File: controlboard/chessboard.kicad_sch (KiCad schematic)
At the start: 9 parts, among them J10 Conn_01x08

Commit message: more progress on controlboard pcb
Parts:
- added D14, D15: WS2812B, LED_SMD:LED_WS2812B_PLCC4_5.0x5.0mm_P3.2mm, symbol LED:WS2812B
- added JP18, JP8: SolderJumper_2_Open, symbol Jumper:SolderJumper_2_Open
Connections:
- net 5V: now also D14.1 (VDD), D15.1 (VDD)
- net GND: now also D14.3 (VSS), D15.3 (VSS)
- net LED_IN: now also D14.4 (DIN), D15.2 (DOUT), JP18.2 (B), JP8.1 (A)
- new net: D14.2 (DOUT), D15.4 (DIN), JP18.1 (A), JP8.2 (B)
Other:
- note added: "3.3V: 64 * 5mA + 8 * 20mA = 480mA"
- note added: "Max: 5V 68 * 36mA = 2.5A Nom: 5V 68 * 12mA = .9A"
- note added: "two more at the end cuz we're cool 😎 + can you ever have too much RGB?"
- note added: "two pixels onboard for debugging/status stuff"

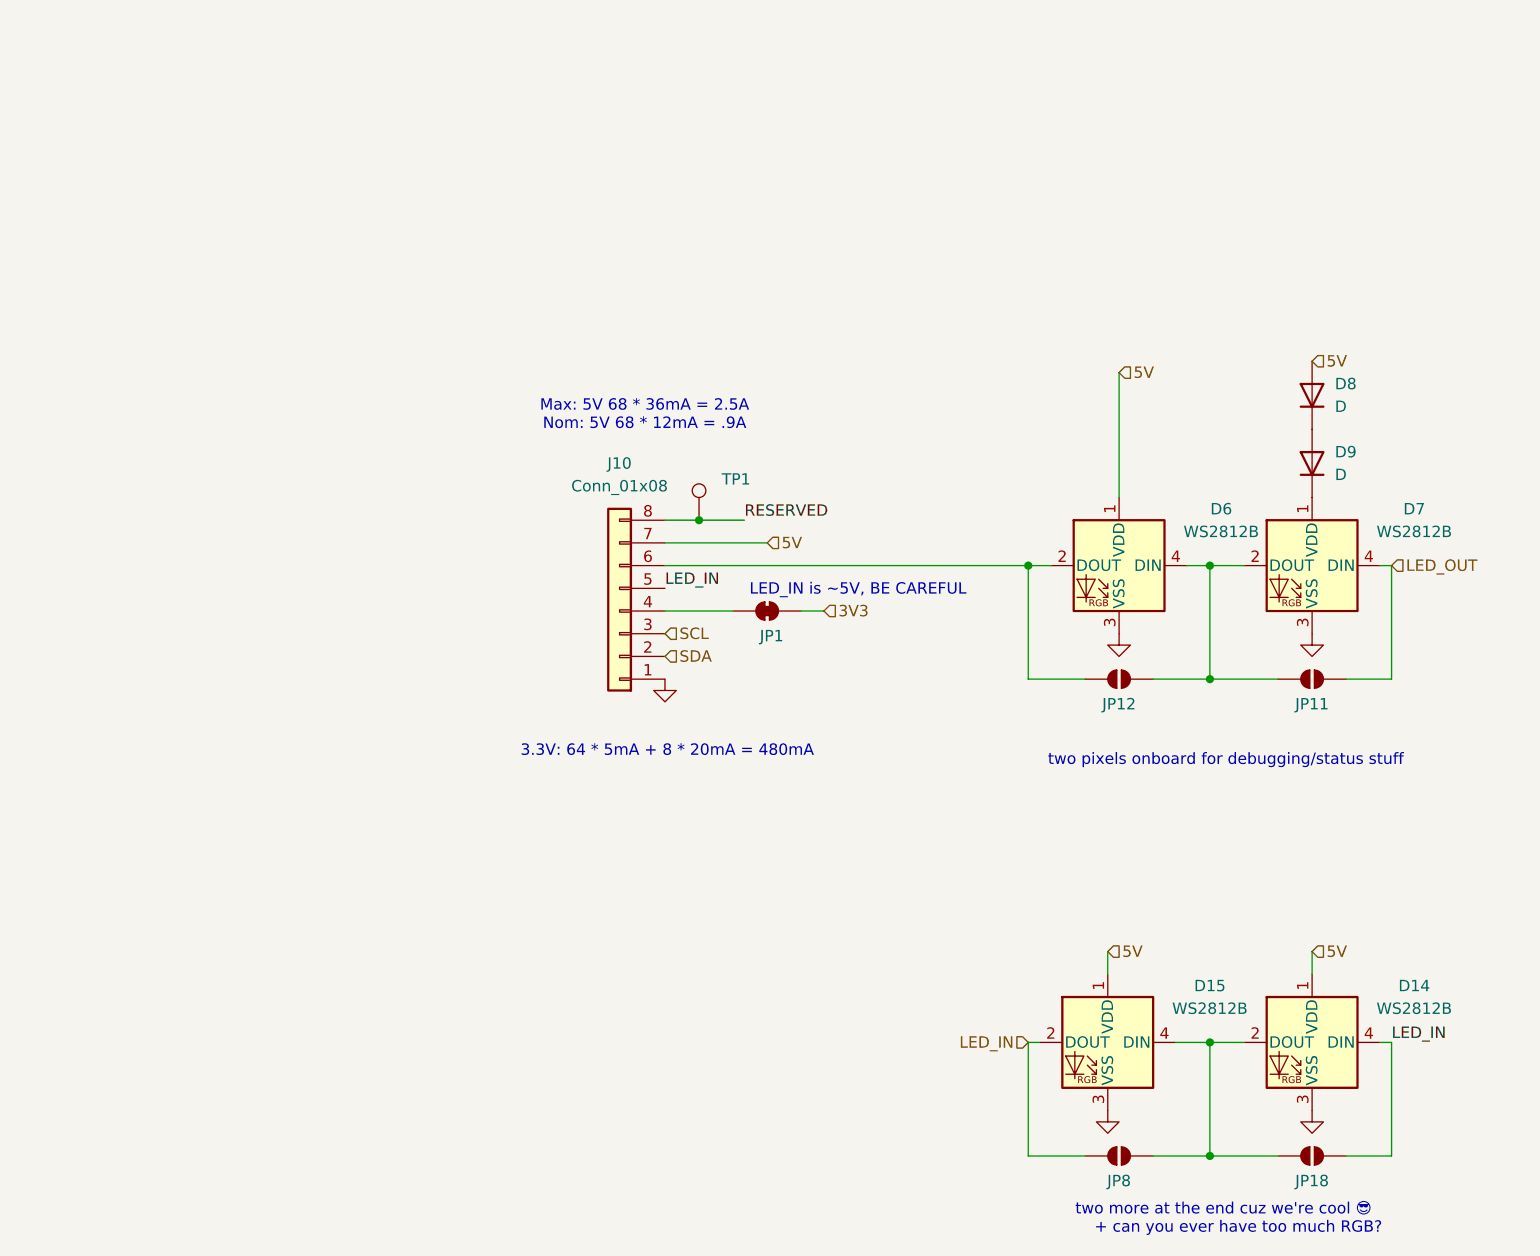
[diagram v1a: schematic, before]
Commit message: ControlBoard Schematic nearly done
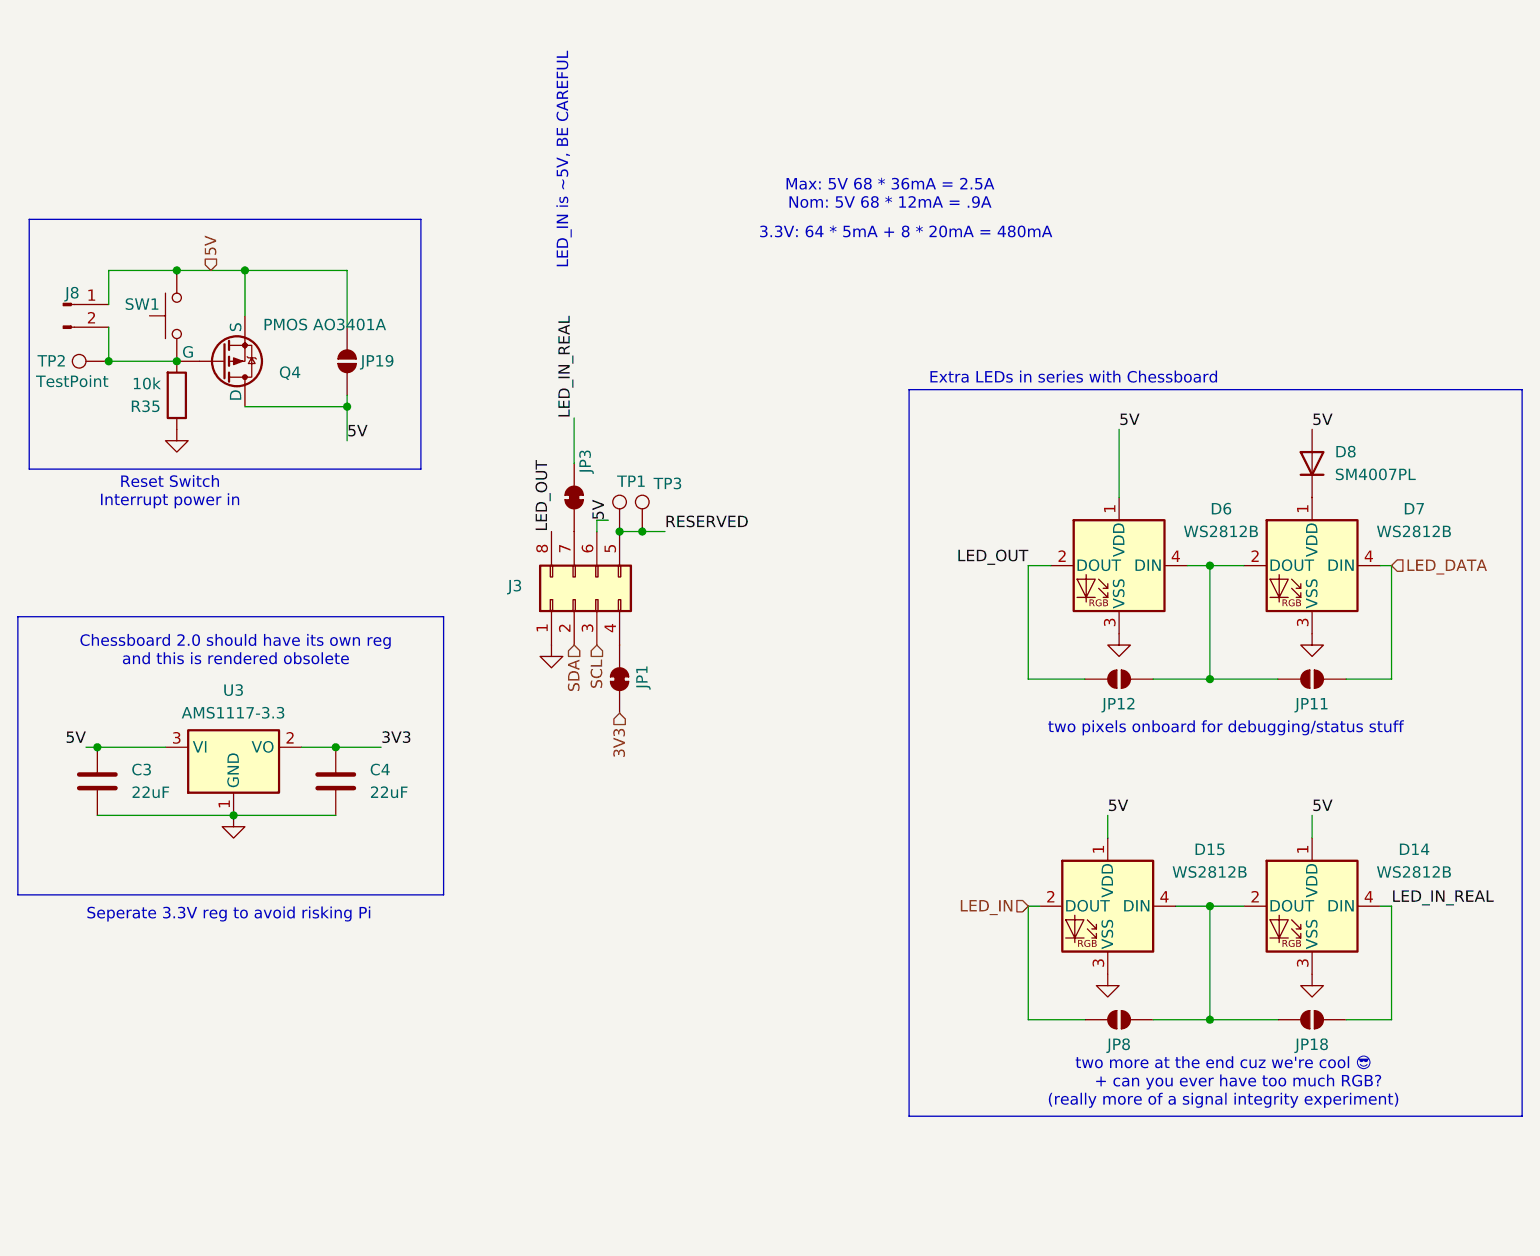
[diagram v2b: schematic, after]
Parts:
- removed D9: D, symbol Device:D
- removed J10: Conn_01x08, symbol Connector_Generic:Conn_01x08
- added C3, C4: 22uF, Capacitor_SMD:C_1206_3216Metric_Pad1.33x1.80mm_HandSolder, symbol Device:C
- added J3: Conn_02x04_Counter_Clockwise, Connector_PinSocket_2.54mm:PinSocket_2x04_P2.54mm_Horizontal, symbol Connector_Generic:Conn_02x04_Counter_Clockwise
- added J8: Conn_01x02_Pin, Connector_PinHeader_2.54mm:PinHeader_1x02_P2.54mm_Vertical, symbol Connector:Conn_01x02_Pin
- added JP19: SolderJumper_2_Open, Jumper:SolderJumper-2_P1.3mm_Open_RoundedPad1.0x1.5mm, symbol Jumper:SolderJumper_2_Open
- added JP3: SolderJumper_2_Bridged, Jumper:SolderJumper-2_P1.3mm_Bridged2Bar_RoundedPad1.0x1.5mm, symbol Jumper:SolderJumper_2_Bridged
- added Q4: PMOS AO3401A, Package_TO_SOT_SMD:SOT-23_Handsoldering, symbol Simulation_SPICE:PMOS
- added R35: 10k, Resistor_SMD:R_0603_1608Metric_Pad0.98x0.95mm_HandSolder, symbol Device:R
- added SW1: SW_Push TODO FP CHECK, Button_Switch_SMD:SW_SPST_SKQG_WithStem, symbol Switch:SW_Push
- added TP2, TP3: TestPoint, Connector_PinSocket_2.54mm:PinSocket_1x01_P2.54mm_Vertical, symbol Connector:TestPoint
- added U3: AMS1117-3.3, Package_TO_SOT_SMD:SOT-223-3_TabPin2, symbol Regulator_Linear:AMS1117-3.3
- D8: value D -> SM4007PL; footprint (none) -> Diode_SMD:Nexperia_CFP3_SOD-123W
- JP1: footprint (none) -> Jumper:SolderJumper-2_P1.3mm_Bridged2Bar_RoundedPad1.0x1.5mm
- JP11, JP12, JP18, JP8: footprint (none) -> Jumper:SolderJumper-2_P1.3mm_Open_RoundedPad1.0x1.5mm
- TP1: footprint (none) -> Connector_PinSocket_2.54mm:PinSocket_1x01_P2.54mm_Vertical
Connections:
- net 3V3: now also C4.1, U3.2 (VO)
- net 5V: now also C3.1, J3.6 (Pin_6), J8.1 (Pin_1), JP19.1 (A), JP19.2 (B), Q4.1 (D), Q4.3 (S), SW1.2, U3.3 (VI)
- net GND: now also C3.2, C4.2, J3.1 (Pin_1), R35.1, U3.1 (GND)
- net LED_IN: no longer D14.4 (DIN), JP18.2 (B)
- net LED_OUT: now also D6.2 (DOUT), JP12.1 (A), J3.8 (Pin_8); no longer D7.4 (DIN), JP11.2 (B)
- net RESERVED: now also J3.5 (Pin_5), TP3.1
- net SCL: now also J3.3 (Pin_3)
- net SDA: now also J3.2 (Pin_2)
- net at JP1.1 (A): now also J3.4 (Pin_4)
- net at D8.1 (K): now also D7.1 (VDD)
- new net: J3.7 (Pin_7), JP3.2 (B)
- new net: J8.2 (Pin_2), Q4.2 (G), R35.2, SW1.1, TP2.1
- new net LED_DATA: D7.4 (DIN), JP11.2 (B)
- new net LED_IN_REAL: D14.4 (DIN), JP18.2 (B), JP3.1 (A)
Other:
- note added: "Chessboard 2.0 should have its own reg and this is rendered obsolete"
- note added: "Extra LEDs in series with Chessboard"
- note added: "Reset Switch Interrupt power in"
- note added: "Seperate 3.3V reg to avoid risking Pi"
- note added: "two more at the end cuz we're cool 😎 + can you ever have too much RGB? (really more of a signal integrity experiment)"
- note removed: "two more at the end cuz we're cool 😎 + can you ever have too much RGB?"
- moved on the sheet: D14, D15, D8, JP1, JP18, JP8, TP1

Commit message: schematic improvements
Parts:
- removed J8: Conn_01x02_Pin, Connector_PinHeader_2.54mm:PinHeader_1x02_P2.54mm_Vertical, symbol Connector:Conn_01x02_Pin
- removed JP19: SolderJumper_2_Open, Jumper:SolderJumper-2_P1.3mm_Open_RoundedPad1.0x1.5mm, symbol Jumper:SolderJumper_2_Open
- removed Q4: PMOS AO3401A, Package_TO_SOT_SMD:SOT-23_Handsoldering, symbol Simulation_SPICE:PMOS
- removed R35: 10k, Resistor_SMD:R_0603_1608Metric_Pad0.98x0.95mm_HandSolder, symbol Device:R
- removed SW1: SW_Push TODO FP CHECK, Button_Switch_SMD:SW_SPST_SKQG_WithStem, symbol Switch:SW_Push
- removed TP2: TestPoint, Connector_PinSocket_2.54mm:PinSocket_1x01_P2.54mm_Vertical, symbol Connector:TestPoint
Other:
- note removed: "Reset Switch Interrupt power in"

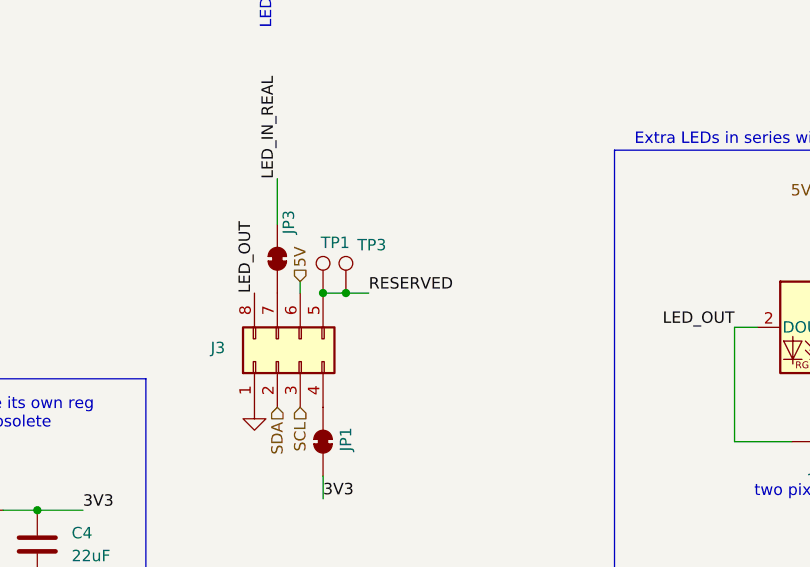
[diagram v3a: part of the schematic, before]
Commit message: improve pinout
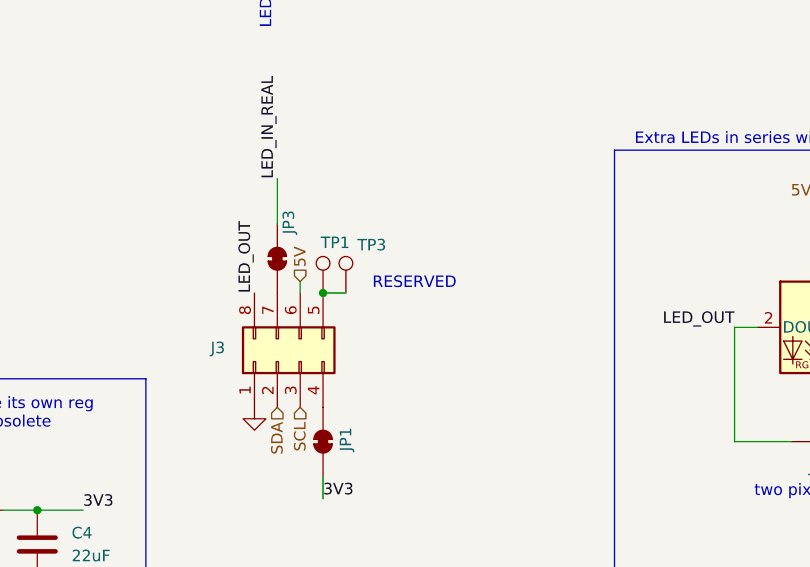
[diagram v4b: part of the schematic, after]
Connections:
- net RESERVED: no longer names the net of J3.5 (Pin_5), TP1.1, TP3.1
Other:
- note added: "RESERVED"
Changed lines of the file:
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@@
 		(color 0 0 0 0)
 	)
-	(junction
-		(at 176.53 71.12)
-		(diameter 0)
-		(color 0 0 0 0)
-	)
 	(wire
 		(pts
@@
 		(pts
 			(xy 233.68 125.73) (xy 240.03 125.73)
-		)
-		(stroke
-			(width 0)
-			(type default)
-		)
-	)
-	(wire
-		(pts
-			(xy 179.07 71.12) (xy 176.53 71.12)
 		)
 		(stroke
@@
 		)
 	)
+	(text "RESERVED"
+		(exclude_from_sim no)
+		(at 184.15 70.104 0)
+		(effects
+			(font
+				(size 1.27 1.27)
+			)
+		)
+	)
 	(text "3.3V: 64 * 5mA + 8 * 20mA = 480mA"
 		(exclude_from_sim no)
@@
 		(fields_autoplaced yes)
 		(effects
-			(font
-				(size 1.27 1.27)
-			)
-			(justify left bottom)
-		)
-	)
-	(label "RESERVED"
-		(at 179.07 71.12 0)
-		(fields_autoplaced yes)
-		(effects

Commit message: progress
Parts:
- removed JP3: SolderJumper_2_Bridged, Jumper:SolderJumper-2_P1.3mm_Bridged2Bar_RoundedPad1.0x1.5mm, symbol Jumper:SolderJumper_2_Bridged
- added C15: 100u, Capacitor_SMD:CP_Elec_6.3x5.4, symbol Device:C_Polarized
- added R12, R21: 1k, Resistor_SMD:R_0603_1608Metric_Pad0.98x0.95mm_HandSolder, symbol Device:R
- J3: symbol Connector_Generic:Conn_02x04_Counter_Clockwise -> Connector_Generic:Conn_02x04_Odd_Even
- TP1, TP3: footprint Connector_PinSocket_2.54mm:PinSocket_1x01_P2.54mm_Vertical -> Connector_PinHeader_1.00mm:PinHeader_1x01_P1.00mm_Vertical
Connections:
- net 5V: now also C15.1
- net GND: now also C15.2
- net LED_IN_REAL: now also R21.2
- net LED_OUT: now also J3.2 (Pin_2), R12.1; no longer D6.2 (DOUT), J3.8 (Pin_8), JP12.1 (A)
- net SCL: now also J3.5 (Pin_5); no longer J3.3 (Pin_3)
- net SDA: now also J3.3 (Pin_3); no longer J3.2 (Pin_2)
- net at JP1.1 (A): now also J3.7 (Pin_7); no longer J3.4 (Pin_4)
- net at TP1.1, TP3.1: now also J3.8 (Pin_8); no longer J3.5 (Pin_5)
- new net: D6.2 (DOUT), JP12.1 (A), R12.2
- new net: J3.4 (Pin_4), R21.1

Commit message: yay its all connected
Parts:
- TP1, TP3: footprint Connector_PinHeader_1.00mm:PinHeader_1x01_P1.00mm_Vertical -> TestPoint:TestPoint_THTPad_1.0x1.0mm_Drill0.5mm
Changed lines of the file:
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@@
 			)
 		)
-		(property "Footprint" "Connector_PinHeader_1.00mm:PinHeader_1x01_P1.00mm_Vertical"
+		(property "Footprint" "TestPoint:TestPoint_THTPad_1.0x1.0mm_Drill0.5mm"
 			(at 179.07 71.12 0)
 			(effects
@@
 			)
 		)
-		(property "Footprint" "Connector_PinHeader_1.00mm:PinHeader_1x01_P1.00mm_Vertical"
+		(property "Footprint" "TestPoint:TestPoint_THTPad_1.0x1.0mm_Drill0.5mm"
 			(at 181.61 71.12 0)
 			(effects

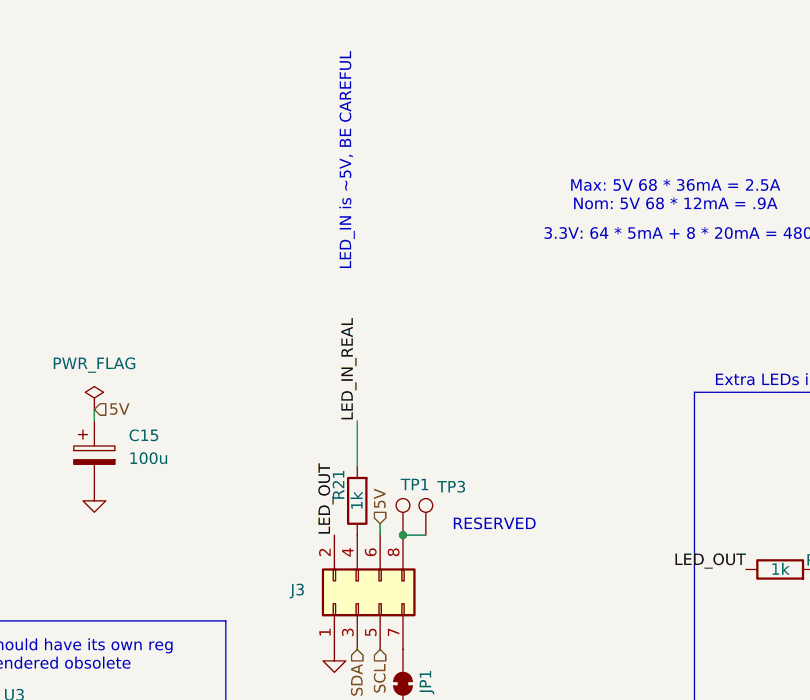
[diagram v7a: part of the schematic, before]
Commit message: controlboard: fix critical mosfet errors
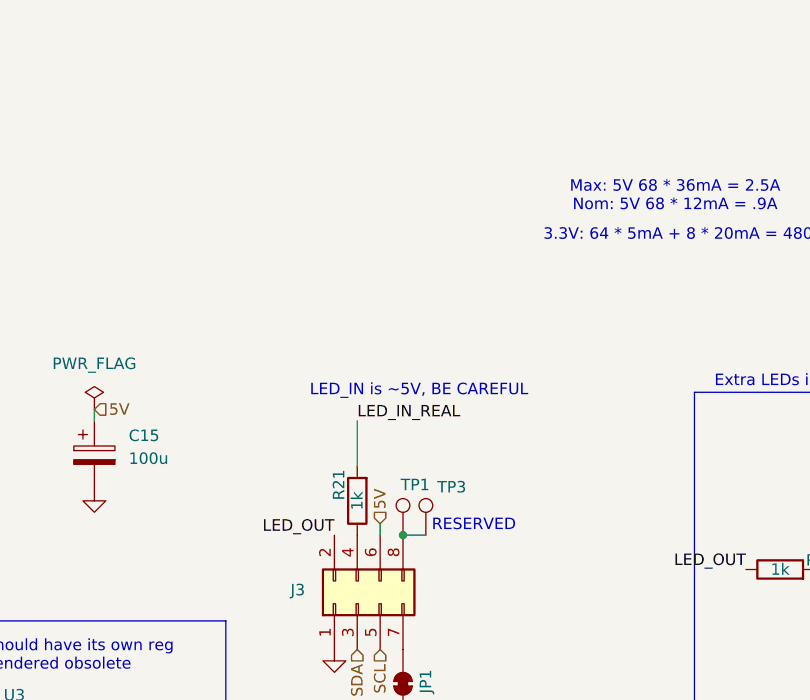
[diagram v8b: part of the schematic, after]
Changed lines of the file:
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@@
 	(text "RESERVED"
 		(exclude_from_sim no)
-		(at 184.15 70.104 0)
+		(at 181.864 70.104 0)
 		(effects
 			(font
@@
 	(text "LED_IN is ~5V, BE CAREFUL"
 		(exclude_from_sim no)
-		(at 167.64 29.718 90)
+		(at 175.768 55.118 0)
 		(effects
 			(font
@@
 	)
 	(label "LED_IN_REAL"
-		(at 168.91 58.42 90)
+		(at 168.91 58.42 0)
 		(fields_autoplaced yes)
 		(effects
@@
 	)
 	(label "LED_OUT"
-		(at 166.37 71.12 90)
+		(at 166.37 71.12 180)
 		(fields_autoplaced yes)
 		(effects
@@
 				(size 1.27 1.27)
 			)
-			(justify left bottom)
+			(justify right bottom)
 		)
 	)
